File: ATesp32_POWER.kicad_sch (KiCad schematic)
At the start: 12 parts, among them J2 JST PH, Q1 DMP2045U, U3 MCP73831-2-OT, U4 AP2112K-3.3

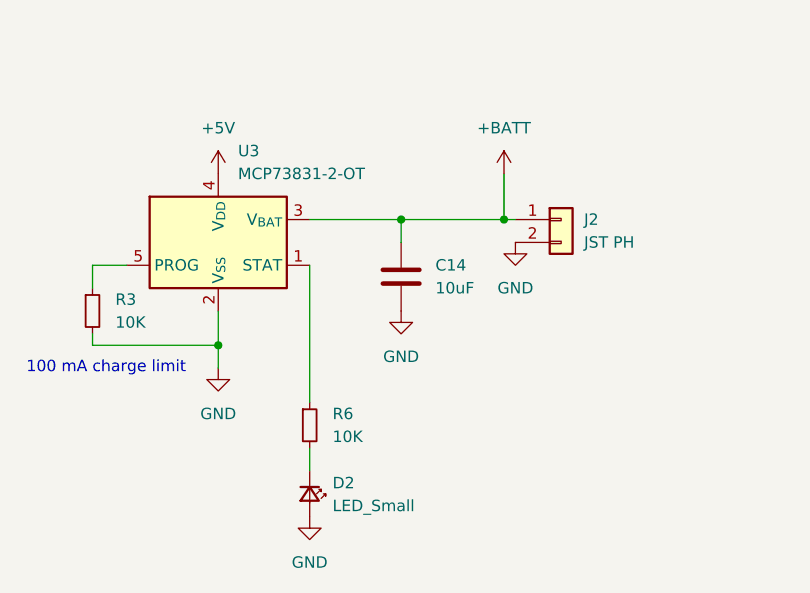
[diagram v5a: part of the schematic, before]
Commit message: fix bug - correct use of open drain status signal of lipo charger
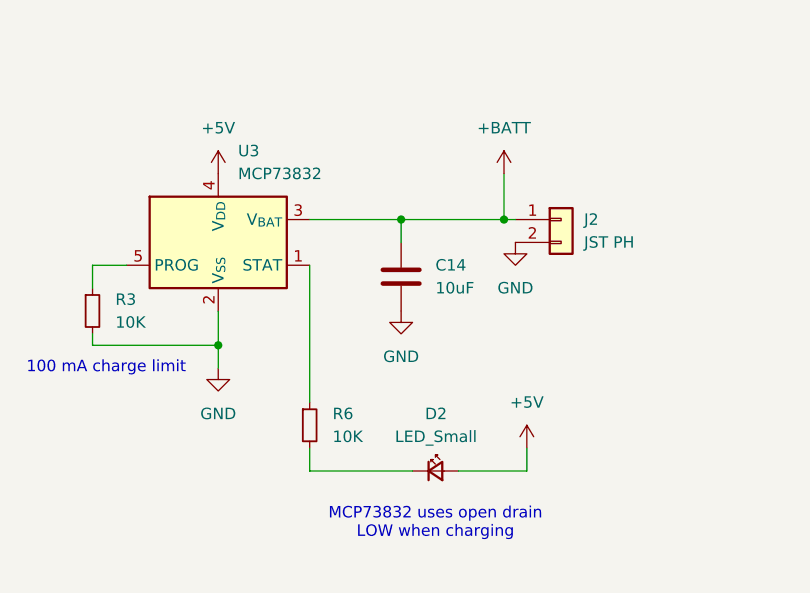
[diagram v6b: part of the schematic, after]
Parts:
- U3: value MCP73831-2-OT -> MCP73832
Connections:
- net +5V: now also D2.2 (A)
- net GND: no longer D2.2 (A)
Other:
- note added: "MCP73832 uses open drain LOW when charging"
- moved on the sheet: D2
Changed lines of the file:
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@@
+	(wire
+		(pts
+			(xy 115.57 149.86) (xy 123.19 149.86)
+		)
+		(stroke
+			(width 0)
+			(type default)
+		)
+	)
 	(wire
 		(pts
@@
 	(wire
 		(pts
+			(xy 99.06 149.86) (xy 110.49 149.86)
+		)
+		(stroke
+			(width 0)
+			(type default)
+		)
+	)
+	(wire
+		(pts
 			(xy 97.79 87.63) (xy 97.79 88.9)
+		)
+		(stroke
+			(width 0)
+			(type default)
+		)
+	)
+	(wire
+		(pts
+			(xy 123.19 149.86) (xy 123.19 147.32)
 		)
 		(stroke
@@
 		)
 	)
+	(text "MCP73832 uses open drain\nLOW when charging"
+		(exclude_from_sim no)
+		(at 113.03 155.702 0)
+		(effects
+			(font
+				(size 1.27 1.27)
+			)
+		)
+	)
 	(symbol
 		(lib_id "Device:LED_Small")
-		(at 99.06 152.4 270)
+		(at 113.03 149.86 0)
 		(unit 1)
 		(exclude_from_sim no)
@@
 		(fields_autoplaced yes)
 		(property "Reference" "D2"
-			(at 101.6 151.1934 90)
-			(effects
-				(font
-					(size 1.27 1.27)
-				)
-				(justify left)
+			(at 113.0935 143.51 0)
+			(effects
+				(font
+					(size 1.27 1.27)
+				)
 			)
 		)
 		(property "Value" "LED_Small"
-			(at 101.6 153.7334 90)
-			(effects
-				(font
-					(size 1.27 1.27)
-				)
-				(justify left)
+			(at 113.0935 146.05 0)
+			(effects
+				(font
+					(size 1.27 1.27)
+				)
 			)
 		)
 		(property "Footprint" "LED_SMD:LED_0402_1005Metric"
-			(at 99.06 152.4 90)
+			(at 113.03 149.86 90)
 			(effects
 				(font
@@
 		)
 		(property "Datasheet" "~"
-			(at 99.06 152.4 90)
+			(at 113.03 149.86 90)
 			(effects
 				(font
@@
 		)
 		(property "Description" "Light emitting diode, small symbol"
-			(at 99.06 152.4 0)
+			(at 113.03 149.86 0)
 			(effects
 				(font
@@
 				(path "/465ced44-ee36-4323-9fa6-a4501ea89ff6/2df8408e-27a9-477c-88a6-1eead4d75269"
 					(reference "D2")
-					(unit 1)
-				)
-			)
-		)
-	)
-	(symbol
-		(lib_id "power:GND")
-		(at 99.06 154.94 0)
-		(unit 1)
-		(exclude_from_sim no)
-		(in_bom yes)
-		(on_board yes)
-		(dnp no)
-		(property "Reference" "#PWR029"
-			(at 99.06 161.29 0)
-			(effects
-				(font
-					(size 1.27 1.27)
-				)
-				(hide yes)
-			)
-		)
-		(property "Value" "GND"
-			(at 99.06 160.02 0)
-			(effects
-				(font
-					(size 1.27 1.27)
-				)
-			)
-		)
-		(property "Footprint" ""
-			(at 99.06 154.94 0)
-			(effects
-				(font
-					(size 1.27 1.27)
-				)
-				(hide yes)
-			)
-		)
-		(property "Datasheet" ""
-			(at 99.06 154.94 0)
-			(effects
-				(font
-					(size 1.27 1.27)
-				)
-				(hide yes)
-			)
-		)
-		(property "Description" "Power symbol creates a global label with name \"GND\" , ground"
-			(at 99.06 154.94 0)
-			(effects
-				(font
-					(size 1.27 1.27)
-				)
-				(hide yes)
-			)
-		)
-		(pin "1"
-		)
-		(instances
-			(project "ATesp32"
-				(path "/465ced44-ee36-4323-9fa6-a4501ea89ff6/2df8408e-27a9-477c-88a6-1eead4d75269"
-					(reference "#PWR029")
 					(unit 1)
 				)
@@
 			)
 		)
-		(property "Value" "MCP73831-2-OT"
+		(property "Value" "MCP73832"
 			(at 91.0941 116.84 0)
 			(effects
@@
 					(unit 1)
 				)
+			)
+		)
+	)
+	(symbol
+		(lib_id "power:+5V")
+		(at 123.19 147.32 0)
+		(unit 1)
+		(exclude_from_sim no)
+		(in_bom yes)
+		(on_board yes)
+		(dnp no)
+		(fields_autoplaced yes)
+		(property "Reference" "#PWR011"
+			(at 123.19 151.13 0)
+			(effects
+				(font
+					(size 1.27 1.27)
+				)
+				(hide yes)
+			)
+		)
+		(property "Value" "+5V"
+			(at 123.19 142.24 0)
+			(effects
+				(font
+					(size 1.27 1.27)
+				)
+			)
+		)
+		(property "Footprint" ""
+			(at 123.19 147.32 0)
+			(effects
+				(font
+					(size 1.27 1.27)
+				)
+				(hide yes)
+			)
+		)
+		(property "Datasheet" ""
+			(at 123.19 147.32 0)
+			(effects
+				(font
+					(size 1.27 1.27)
+				)
+				(hide yes)
+			)
+		)
+		(property "Description" "Power symbol creates a global label with name \"+5V\""
+			(at 123.19 147.32 0)
+			(effects
+				(font
+					(size 1.27 1.27)
+				)
+				(hide yes)
+			)
+		)
+		(pin "1"
+		)
+		(instances
+			(project "ATesp32"
+				(path "/465ced44-ee36-4323-9fa6-a4501ea89ff6/2df8408e-27a9-477c-88a6-1eead4d75269"
+					(reference "#PWR011")
+					(unit 1)
+				)

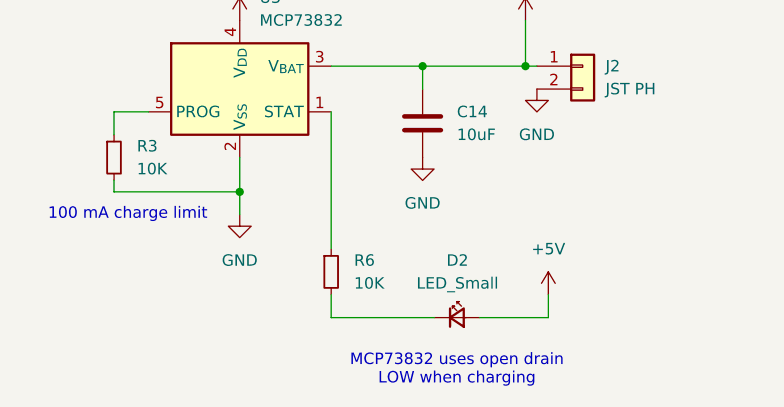
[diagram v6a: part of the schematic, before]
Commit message: spec components for JLC
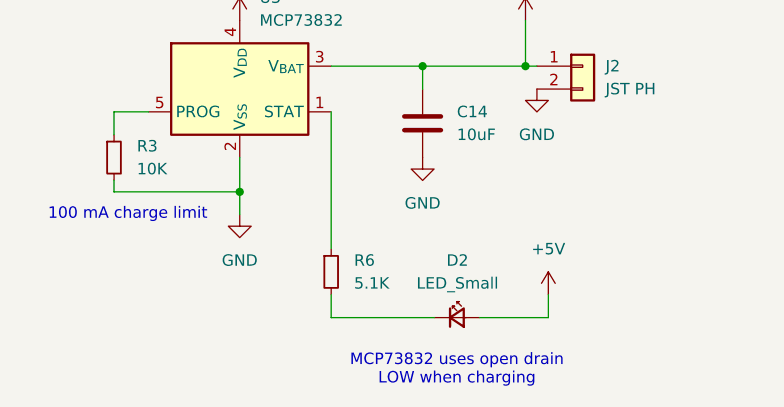
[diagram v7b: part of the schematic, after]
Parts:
- C13, C14: JLC (none) -> C315248
- D2: JLC (none) -> C510300
- D4: JLC (none) -> C48192
- J2: JLC (none) -> C295747
- Q1: JLC (none) -> C459541
- R2, R4: JLC (none) -> C25741
- R3: JLC (none) -> C25744
- R6: value 10K -> 5.1K; JLC (none) -> C25905
- U3: JLC (none) -> C38066
- U4: JLC (none) -> C51118

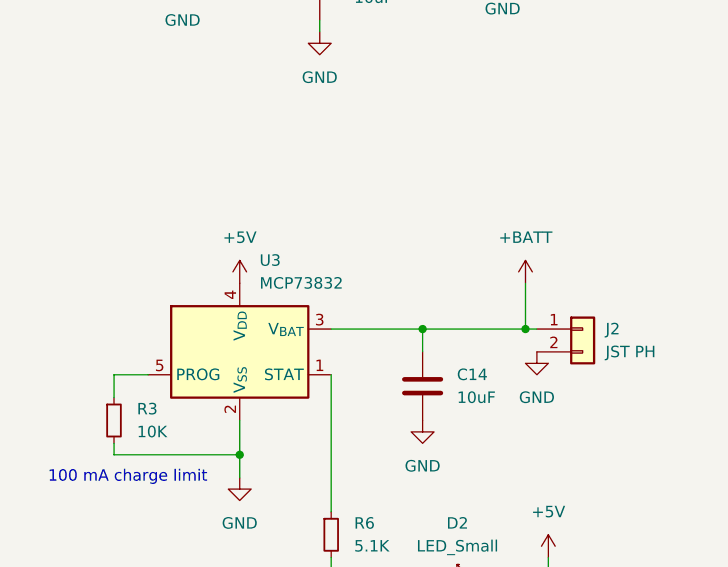
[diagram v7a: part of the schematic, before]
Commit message: Generate production files. More clear part names for ESP and LiPo charger
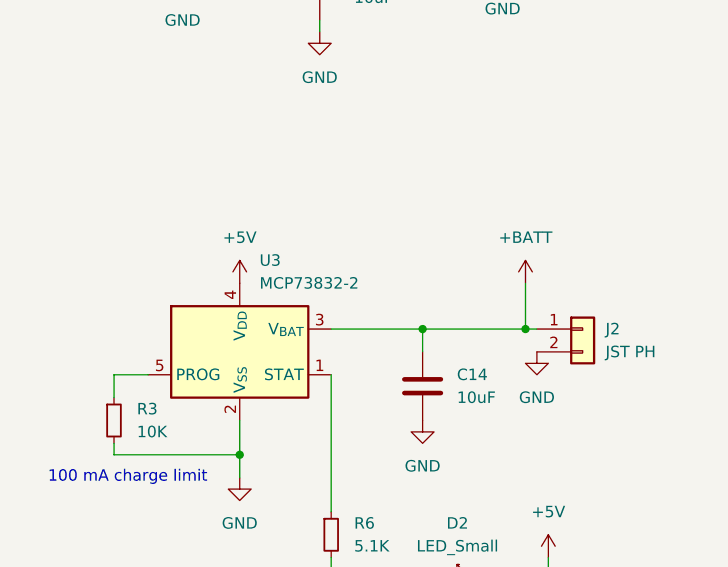
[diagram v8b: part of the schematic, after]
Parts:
- U3: value MCP73832 -> MCP73832-2
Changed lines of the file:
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@@
 			)
 		)
-		(property "Value" "MCP73832"
+		(property "Value" "MCP73832-2"
 			(at 91.0941 116.84 0)
 			(effects
